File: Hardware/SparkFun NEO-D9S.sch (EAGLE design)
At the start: 47 parts, among them J1 ANTENNA-SMA-GROUNDEDEDGE_SMA, J2 Qwiic Right Angle, J4 Qwiic Right Angle, U1 U-BLOX_NEO-D9S, U2 3.3V

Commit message: Routed. Add schematic
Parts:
- removed JP5: JUMPER-SMT_3_2-NC_TRACE_SILK, SparkFun-Jumpers:JUMPER-SMT_3_2-NC_TRACE_SILK
- added I2C: JUMPER-SMT_3_NO_SILK, SparkFun-Jumpers:JUMPER-SMT_3_NO_SILK
- added LOGO3: SFE_LOGO_NAME_FLAME.1_INCH, SparkFun-Aesthetics:SFE_LOGO_NAME_FLAME.1_INCH
- added LOGO4: OSHW-LOGOS, SparkFun-Aesthetics:OSHW-LOGOS
- J3: device SparkFun-Connectors:USB_C2-LAYER -> SparkFun-Connectors:USB_C_2-LAYER_PADS
- LOGO1: value OSHW-LOGOMINI -> OSHW-LOGOS; device SparkFun-Aesthetics:OSHW-LOGOMINI -> SparkFun-Aesthetics:OSHW-LOGOS
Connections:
- net 3.3V: now also I2C.2; no longer JP5.2
- net D+: now also D2.6; no longer D2.4
- net D-: now also D2.4; no longer D2.6
- net N$5: now also I2C.1; no longer JP5.1
- net N$8: now also I2C.3; no longer JP5.3
- net USB_D+: now also D2.1; no longer D2.3
- net USB_D-: now also D2.3; no longer D2.1
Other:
- note added: "50Ω"
- note added: "Close jumper to add I2C pullups to bus"
- note removed: "Cut jumper to remove I2C pullups from bus"
- moved on the sheet: C1, D1, D2, FB1, J1, J2, J5, LED1, PWR\, R1, R14, R7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

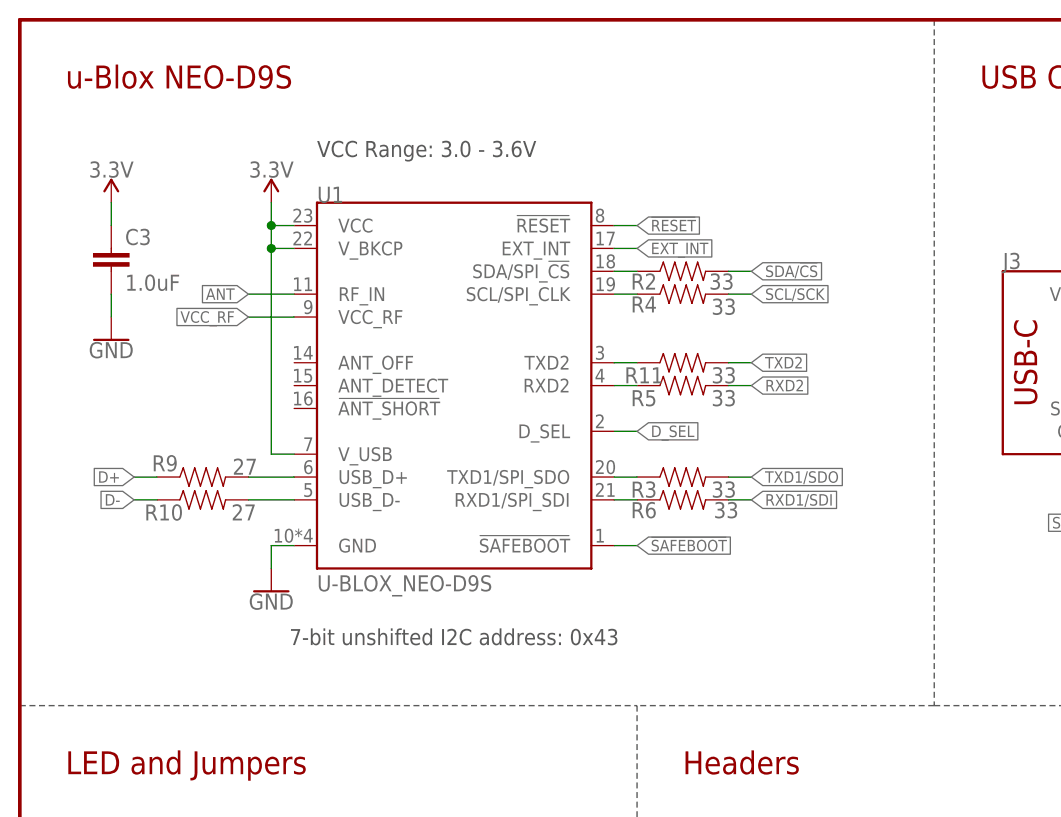
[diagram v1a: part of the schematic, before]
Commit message: Add C6
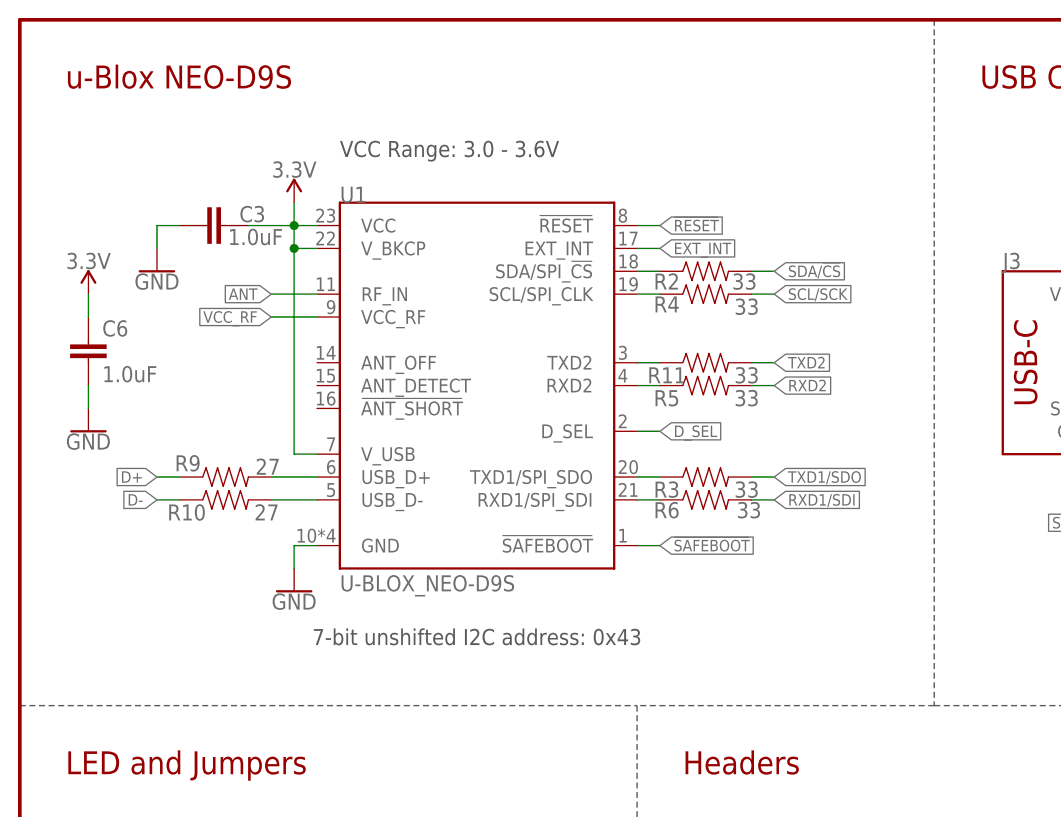
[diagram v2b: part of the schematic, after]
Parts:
- added C6: 1.0uF, SparkFun-Capacitors:1.0UF-0603-16V-10%
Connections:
- net 3.3V: now also C6.1
- net GND: now also C6.2
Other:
- moved on the sheet: C3, R10, R11, R2, R3, R4, R5, R6, R9, U1

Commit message: Add cut marks for antenna power
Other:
- note added: "90Ω"
- note added: "Cut track to disable active antenna power"
- moved on the sheet: C1, C6, D1, FB1, J1, R14

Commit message: Post-Proto Review Changes
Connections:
- net RXD1/SDI renamed RXD1/PICO
- net TXD1/SDO renamed TXD1/POCI
- removed net N$13: R3.1, U1.TXD1/SPI_SDO
- new net N$6: R6.1, U1.RXD1/PICO
- net N$2: now also R3.1, U1.TXD1/POCI; no longer R6.1, U1.RXD1/SPI_SDI
- net N$3: now also U1.SDA/!CS!; no longer U1.SDA/SPI_!CS!
- net N$4: now also U1.SCL/SCK; no longer U1.SCL/SPI_CLK
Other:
- moved on the sheet: C3, C6, R10, R11, R2, R3, R4, R5, R6, R9, U1

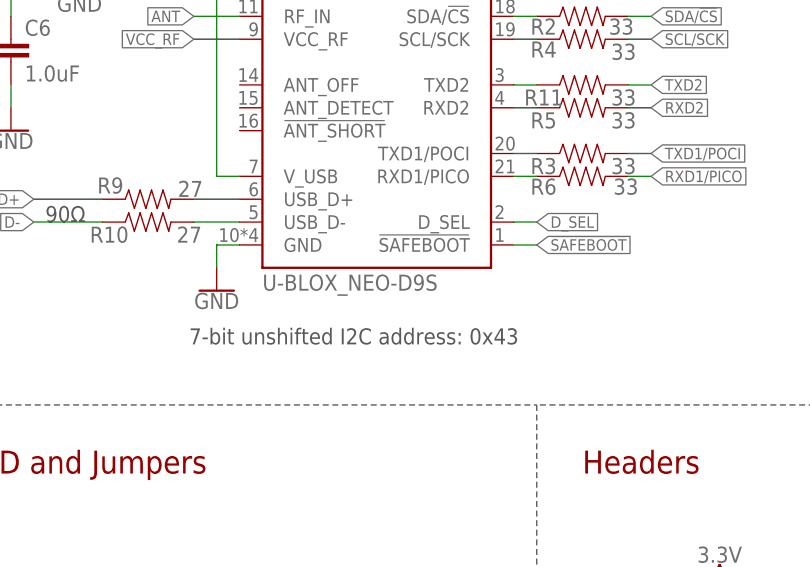
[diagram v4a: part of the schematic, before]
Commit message: Add PROD_ID for NEO-D9S-00B. Add Proto production files
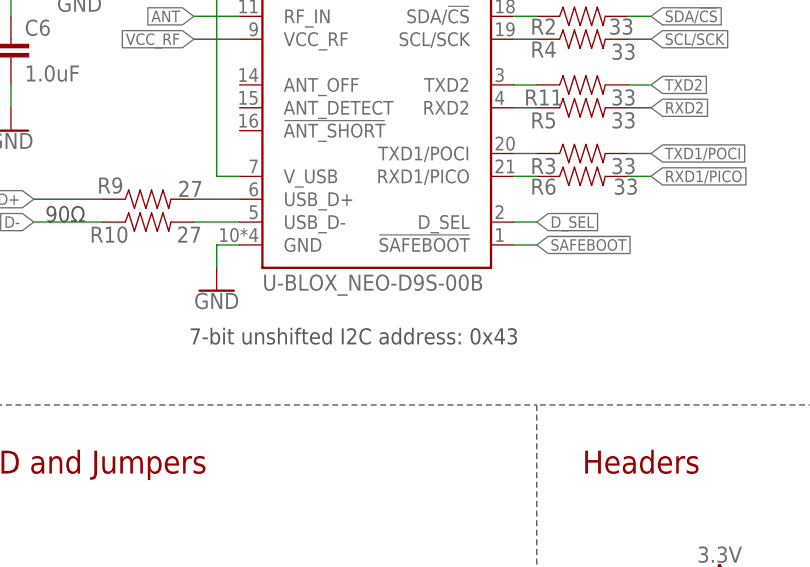
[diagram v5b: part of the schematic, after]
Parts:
- U1: value U-BLOX_NEO-D9S -> U-BLOX_NEO-D9S-00B; device SparkFun-GPS:U-BLOX_NEO-D9S -> SparkFun-GPS:U-BLOX_NEO-D9S-00B
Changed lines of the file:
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@@
 <part name="GND2" library="SparkFun-PowerSymbols" deviceset="GND" device=""/>
 <part name="SUPPLY10" library="SparkFun-PowerSymbols" deviceset="3.3V" device=""/>
-<part name="U1" library="SparkFun-GPS" deviceset="U-BLOX_NEO-D9S" device=""/>
+<part name="U1" library="SparkFun-GPS" deviceset="U-BLOX_NEO-D9S" device="-00B"/>
 </parts>
 <sheets>

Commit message: Updates for v10 PCB
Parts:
- added 3V3: JUMPER-SMT_2_NC_TRACE_SILK, SparkFun-Jumpers:JUMPER-SMT_2_NC_TRACE_SILK
- added C7: 47pF, SparkFun-Capacitors:47PF-0603-50V-5%
- added R15: DNP, SparkFun-Resistors:DNP-0603_NO_CREAM
- J7: device SparkFun-Connectors:CONN_09NO_SILK -> SparkFun-Connectors:CONN_10NO_SILK_PTH_FEMALE
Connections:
- new net ANT_PWR: J7.10, R15.2
- new net N$13: 3V3.1, J5.3
- new net SMA: C7.1, D1.1, FB1.1, J1.SIGNAL, R15.1
- net 3.3V: now also 3V3.2
- net ANT: now also C7.2; no longer D1.1, FB1.1, J1.SIGNAL
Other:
- note added: "Cut track to disable VCC_RF antenna power"
- note added: "v10"
- note removed: "Cut track to disable active antenna power"
- note removed: "v01"
- moved on the sheet: C1, FB1, J1, R14

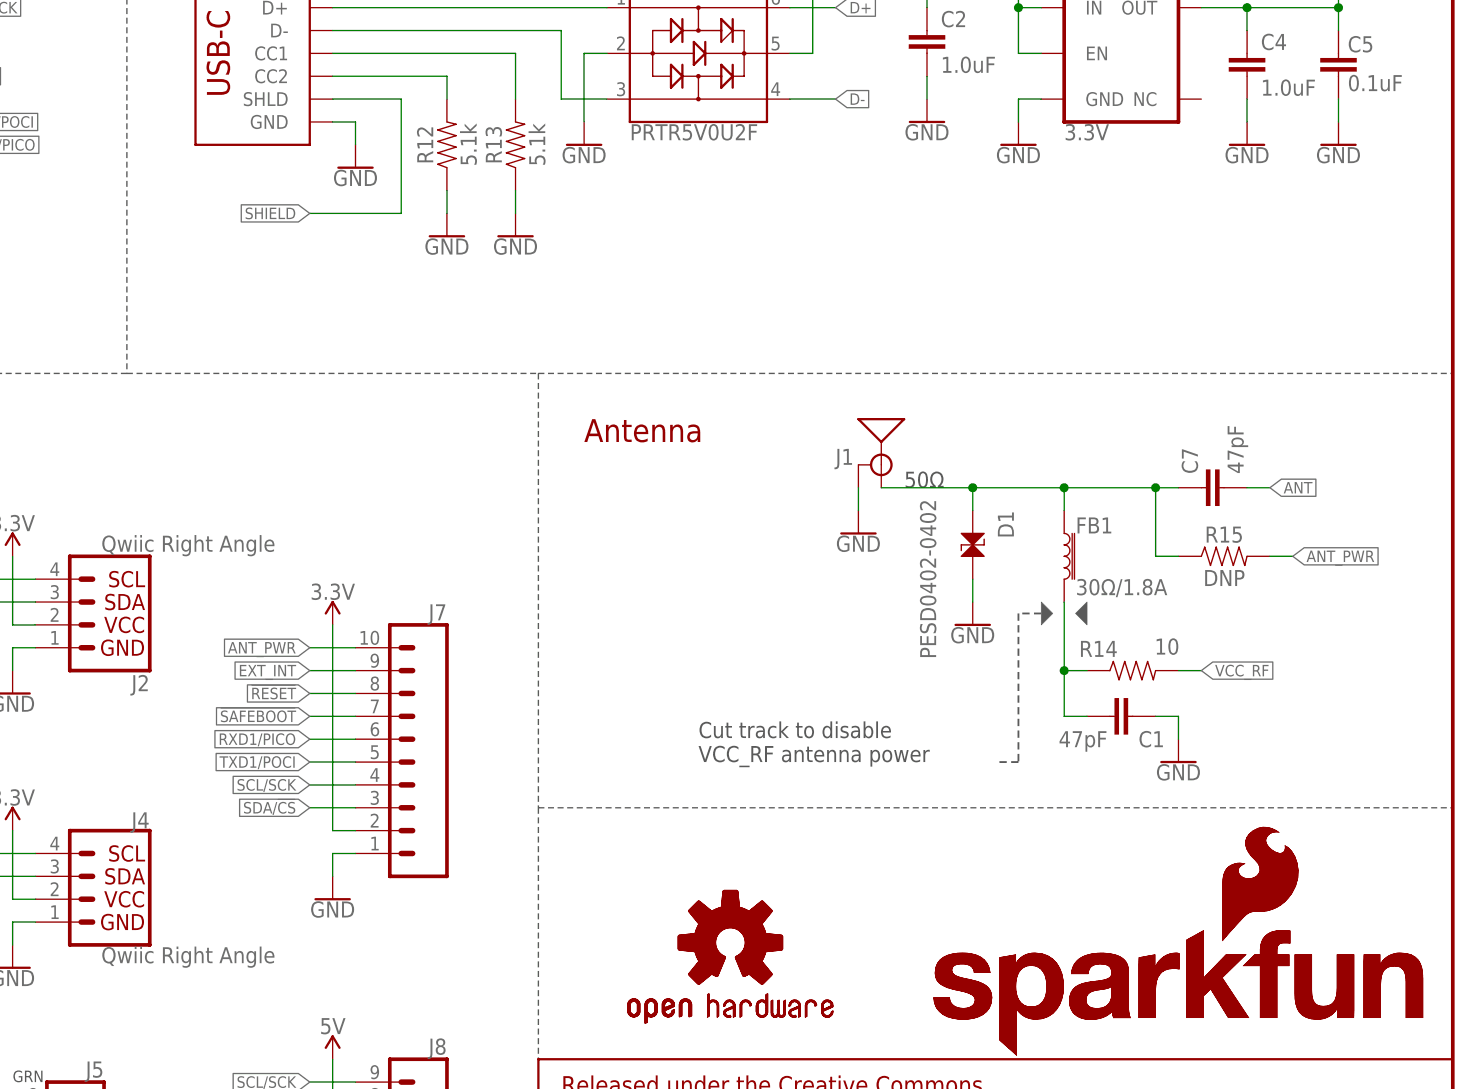
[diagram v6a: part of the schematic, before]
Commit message: Updates after REDs Review
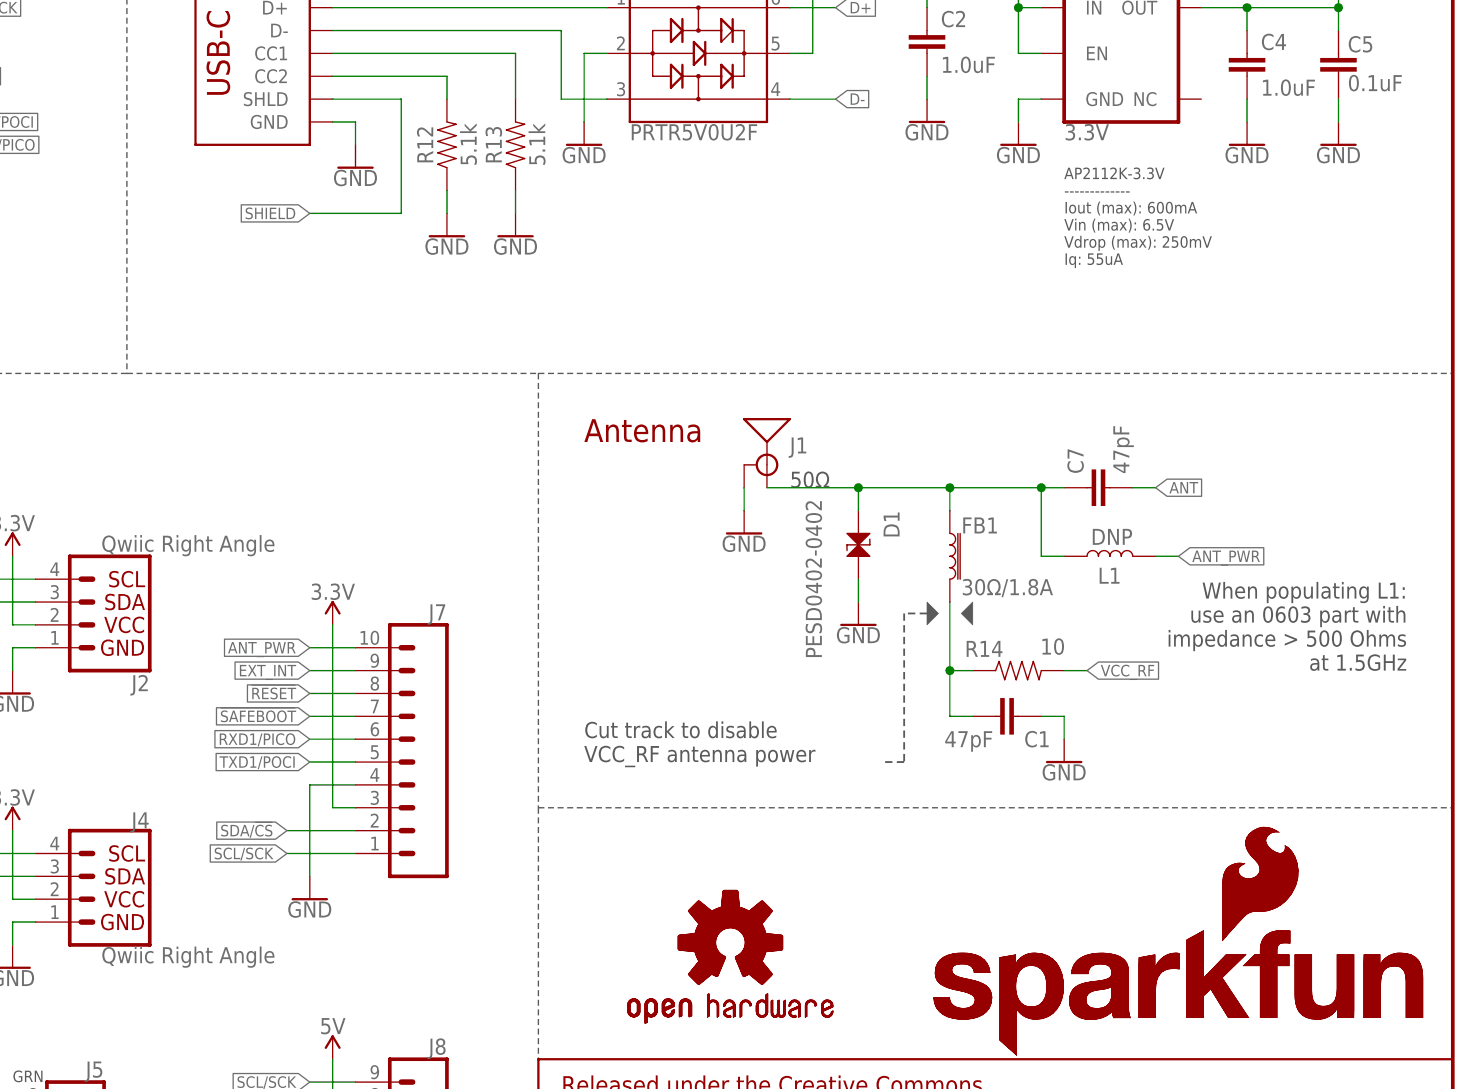
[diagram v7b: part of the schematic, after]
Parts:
- removed R15: DNP, SparkFun-Resistors:DNP-0603_NO_CREAM
- added L1: DNP, SparkFun-Coils:DNP-0603_NO-CREAM
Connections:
- net 3.3V: now also J7.3; no longer J7.2
- net ANT_PWR: now also L1.2; no longer R15.2
- net GND: now also J7.4; no longer J7.1
- net SCL/SCK: now also J7.1; no longer J7.4
- net SDA/!CS!: now also J7.2; no longer J7.3
- net SMA: now also L1.1; no longer R15.1
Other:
- note added: "AP2112K-3.3V ------------- Iout (max): 600mA Vin (max): 6.5V Vdrop (max): 250mV Iq: 55uA"
- note added: "When populating L1: use an 0603 part with impedance > 500 Ohms at 1.5GHz"
- moved on the sheet: C1, C7, D1, FB1, J1, R14

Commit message: Update schematic
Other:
- note added: "u-blox NEO-D9S"
- note removed: "u-Blox NEO-D9S"
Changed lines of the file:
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@@
 <text x="73.66" y="104.14" size="2.54" layer="94" font="vector">Headers</text>
 <text x="5.08" y="104.14" size="2.54" layer="94" font="vector">LED and Jumpers</text>
-<text x="5.08" y="177.8" size="2.54" layer="94" font="vector">u-Blox NEO-D9S</text>
+<text x="5.08" y="177.8" size="2.54" layer="94" font="vector">u-blox NEO-D9S</text>
 <wire x1="68.58" y1="111.76" x2="68.58" y2="0" width="0.1524" layer="97" style="shortdash"/>
 <wire x1="40.64" y1="53.34" x2="45.72" y2="53.34" width="0.2032" layer="97" style="dashdot"/>
